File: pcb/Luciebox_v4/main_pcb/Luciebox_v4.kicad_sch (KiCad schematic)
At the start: 67 parts, among them J1 USB_B_Mini, P1 Power, P2 Analog, P3 Digital, P4 Digital, P5 CONN_01X01, P6 CONN_01X01, P7 CONN_01X01, P8 CONN_01X01, Q1 N-Channel_Mosfet, T1 terminal_3x1, T10 terminal_8x1, T11 terminal_8x1, T12 terminal_8x1, T13 terminal_8x1, T2 terminal_3x1, T3 terminal_3x1, T4 terminal_3x1, T5 terminal_8x1, T6 terminal_8x1, T7 terminal_3x1, T8 terminal_3x1, T9 terminal_3x1, U1 CA56-12SRWA, U2 8X8PADS, U3 ATmega328-PU, Y1 16MHz

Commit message: V4 main pcb ready for layouting
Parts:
- removed P1: Power, Socket_Arduino_Uno:Socket_Strip_Arduino_1x08, symbol Luciebox_components:Conn_01x08-Connector_Generic
- removed P2: Analog, Socket_Arduino_Uno:Socket_Strip_Arduino_1x06, symbol Luciebox_components:Conn_01x06-Connector_Generic
- removed P3: Digital, Socket_Arduino_Uno:Socket_Strip_Arduino_1x10, symbol Luciebox_components:Conn_01x10-Connector_Generic
- removed P4: Digital, Socket_Arduino_Uno:Socket_Strip_Arduino_1x08, symbol Luciebox_components:Conn_01x08-Connector_Generic
- removed P5, P6, P7, P8: CONN_01X01, Socket_Arduino_Uno:Arduino_1pin, symbol Luciebox_components:Conn_01x01-Connector_Generic
- removed Q1: N-Channel_Mosfet, Luciebox:TO-220-3, symbol Luciebox_components:N-Channel_Mosfet
- removed R1, R11, R12, R13, R14, R2, R3, R4, R5, R6, R7, R8, R9: 10K, Luciebox:1206_0805, symbol Luciebox_components:R_Small-Device
- removed R10: 100K, Luciebox:1206_0805, symbol Luciebox_components:R_Small-Device
- removed R_0_if_no_touch1: 0, Luciebox:1206_0805, symbol Luciebox_components:R_Small-Device
- removed S2: selector_knob, Luciebox:Rotary_Switch, symbol Luciebox_components:selector_knob
- removed T10, T11: terminal_8x1, Luciebox:Terminal_8x1_100mil, symbol Luciebox_components:terminal_8x1
- removed T2, T3, T4, T7, T8: terminal_3x1, Luciebox:Terminal_3x1_100mil, symbol Luciebox_components:terminal_3x1
- removed TP1: TestPoint_Probe, symbol Connector:TestPoint_Probe
- added A1: Arduino_UNO_R3, Module:Arduino_UNO_R3, symbol Luciebox_components:Arduino_UNO_R3
- added D1, D10, D2, D3, D4, D5, D6, D7, D8: D_Schottky, Luciebox:D_SMA, symbol Luciebox_components:D_Schottky
- added Q1: P-Channel MOSFET, Package_TO_SOT_SMD:SOT-23, symbol Luciebox_components:P-Channel MOSFET
- added Q2: NPN transistor, Luciebox:SOT-23, symbol Luciebox_components:NPN transistor
- added R10, R11, R12, R13, R15, R16, R17, R18, R20, R21, R22, R23, R6, R7, R8, R9: R_Small, Luciebox:0603_1608Metric, symbol Luciebox_components:R_Small
- added R25, R28: 100K, Luciebox:0603_1608Metric, symbol Luciebox_components:R_Small-Device
- added R26: 1K, Luciebox:0603_1608Metric, symbol Luciebox_components:R_Small-Device
- added R27: 10K, Luciebox:0603_1608Metric, symbol Luciebox_components:R_Small-Device
- added R_0_if_no_auto_power_off1: 0, Luciebox:0603_1608Metric, symbol Luciebox_components:R_Small-Device
- added T6: terminal_8x1, Luciebox:Terminal_8x1_100mil, symbol Luciebox_components:terminal_8x1
- C1, C2, C3: footprint Luciebox:0805 -> Luciebox:0603_1608Metric
- D9: renamed from D1; footprint Luciebox:smd_throughhole_2_pins -> Luciebox:D_SMA
- R1: renamed from R15; footprint Luciebox:1206_0805 -> Luciebox:0603_1608Metric
- R19: renamed from R20; footprint Luciebox:1206_0805 -> Luciebox:0603_1608Metric
- R2: renamed from R16; footprint Luciebox:1206_0805 -> Luciebox:0603_1608Metric
- R3: renamed from R17; footprint Luciebox:1206_0805 -> Luciebox:0603_1608Metric
- R4: renamed from R18; footprint Luciebox:1206_0805 -> Luciebox:0603_1608Metric
- R5: renamed from R19; footprint Luciebox:1206_0805 -> Luciebox:0603_1608Metric
- R_0_if_no_usb_switch1, R_reset_pullup1, R_vcc_protected1: footprint Luciebox:1206_0805 -> Luciebox:0603_1608Metric
- renumbered H5 to H2, H6 to H3, H2 to H4, H3 to H5, H7 to H6, H4 to H7, T5 to T1, T1 to T2, T6 to T4, T9 to T5, T13 to T7, T12 to T8
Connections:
- net +3V3: now also A1.4 (3V3)
- net 0(Rx): now also A1.15 (D0/RX), D5.1 (K); no longer T1.5
- net 1(Tx): now also A1.16 (D1/TX), D6.1 (K); no longer T4.6
- net 10(PWM-SS): now also A1.25 (D10)
- net 11(PWM-MOSI): now also A1.26 (D11)
- net 12(MISO): now also A1.27 (D12), D8.1 (K); no longer T1.7
- net 13(SCK): now also A1.28 (D13), D7.1 (K); no longer T4.8
- net 2: now also A1.17 (D2)
- net 3(PWM): now also A1.18 (D3)
- net 4: now also A1.19 (D4), D3.1 (K); no longer T4.7
- net 5(PWM): now also A1.20 (D5)
- net 6(PWM): now also A1.21 (D6)
- net 7: now also A1.22 (D7), D1.1 (K); no longer T1.8
- net 8: now also A1.23 (D8), D4.1 (K); no longer T1.6
- net 9(PWM): now also A1.24 (D9)
- net A0: now also A1.9 (A0), T6.6
- net A1: now also A1.10 (A1), R15.1, R20.1; no longer T1.3
- net A2: now also A1.11 (A2), R10.1, R6.1; no longer T4.3
- net A3: now also A1.12 (A3), D2.1 (K); no longer T4.5
- net A4(SDA): now also A1.13 (SDA/A4), A1.31 (SDA/A4)
- net A5(SCL): now also T2.3, A1.14 (SCL/A5), A1.32 (SCL/A5)
- net AREF: now also A1.30 (AREF)
- net GND: now also T8.7, A1.29 (GND), A1.6 (GND), A1.7 (GND), Q2.3 (E), R13.2, R23.2, R28.1, T6.1, T6.4; no longer T1.1, T2.3, T4.1, T8.8
- net IOREF: now also A1.2 (IOREF)
- net Reset: now also A1.3 (~{RESET})
- net VCC: now also T8.8, Q1.3 (D), R_0_if_no_auto_power_off1.1, T6.2; no longer R_0_if_no_usb_switch1.2, T8.1, T8.6
- net VCC_minimalCurrent: no longer T1.2, T4.2
- net Vin: now also R_0_if_no_usb_switch1.2, T8.1, T8.6, A1.8 (VIN), Q1.2 (S), R25.1, R_0_if_no_auto_power_off1.2
- net at T8.3: now also D10.2 (A), T6.5; no longer T8.5
- new net: D8.2 (A), T1.8
- new net: Q2.2 (B), R26.1, R27.2
- new net: R26.2, T6.7
- new net: Q1.1 (G), Q2.1 (C), R25.2
- new net: R18.2, T4.1
- new net: R17.2, T4.2
- new net: R16.2, T4.3
- new net: R15.2, T4.4
- new net: R9.2, T4.5
- new net: R8.2, T4.6
- new net: R7.2, T4.7
- new net: R6.2, T4.8
- new net: D6.2 (A), T1.6
- new net: R17.1, R21.2, R22.1
- new net: D1.2 (A), T1.1
- new net: D2.2 (A), T1.2
- new net: D3.2 (A), T1.3
- new net: D4.2 (A), T1.4
- new net: D5.2 (A), T1.5
- new net: D7.2 (A), T1.7
- new net: R12.2, R13.1, R9.1
- new net: R18.1, R22.2, R23.1
- new net: R11.2, R12.1, R8.1
- new net: R16.1, R20.2, R21.1
- new net: R10.2, R11.1, R7.1
- new net: D10.1 (K), T8.5
- new net: R1.1, T6.3
- new net 5V arduino: A1.5 (+5V)
- new net A4: R27.1, R28.2
- no-connect marks 5 -> 0
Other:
- removed sheet Luciebox_buttons
- note added: "Arduino UNO R3 Footprint"
- note added: "Button lights Common Anode"
- note removed: "1"
- note removed: "GND-SWITCHED"
- note removed: "Holes"
- note removed: "Shield for Arduino that uses the same pin disposition like "Uno" board Rev 3."
- note removed: "Touch ON and Auto power OFF"
- moved on the sheet: BZ1, C1, D9, H1, H2, H3, H4, H5, H6, H7, H8, J1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

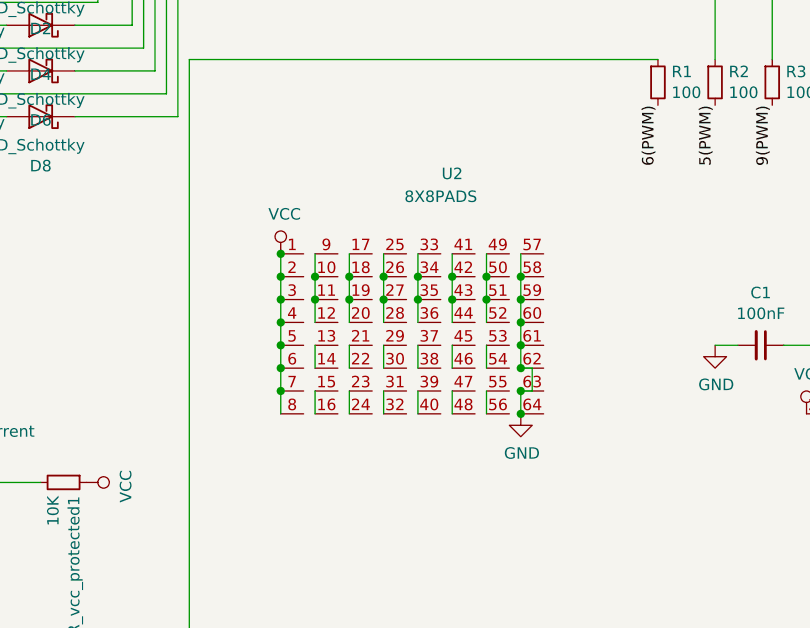
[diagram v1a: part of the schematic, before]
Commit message: layout main board start
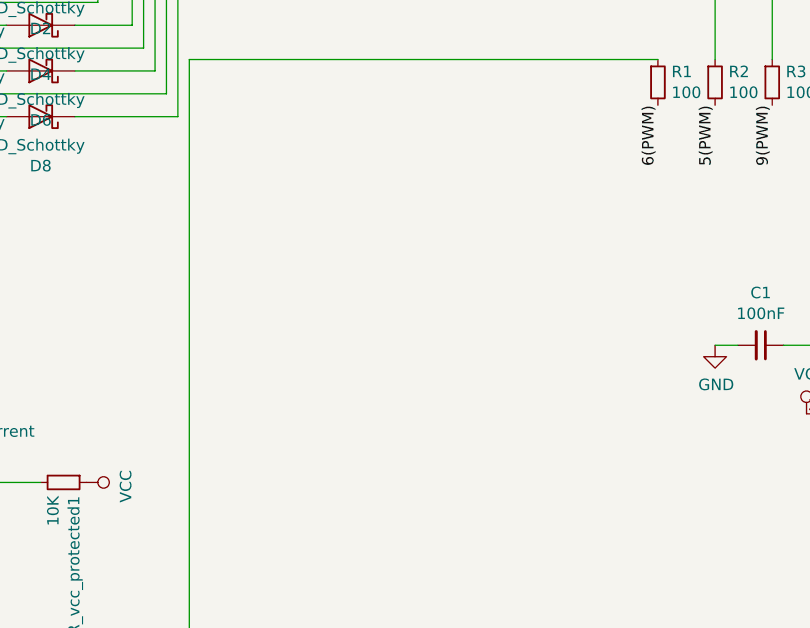
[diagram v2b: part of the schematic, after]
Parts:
- removed U2: 8X8PADS, Luciebox:64_PADS_100mil, symbol Luciebox_components:8X8PADS

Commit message: Pcb v4 evolution
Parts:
- added J2: USB_B_Mini, Luciebox:usb_mini_Molex-0548190519, symbol Luciebox_components:USB_B_Mini
- A1: footprint Module:Arduino_UNO_R3 -> Module:Arduino_UNO_R3_WithMountingHoles
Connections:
- net A4: now also R27.2; no longer R27.1, R28.2
- net GND: now also J2.1 (GND), J2.6 (Shield)
- net at Q2.2 (B), R26.1: now also R27.1, R28.2; no longer R27.2
- net at J1.2 (ID), T5.1: now also J2.2 (ID)
- net at J1.3 (D+), T5.3: now also J2.3 (D+)
- net at J1.4 (D-), T5.2: now also J2.4 (D-)
- net at D9.2 (A), J1.5 (VBUS): now also J2.5 (VBUS)
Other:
- moved on the sheet: R27, T5

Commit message: Delete Arduino Uno footprint. Line up bottonboard and main pcb
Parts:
- removed A1: Arduino_UNO_R3, Module:Arduino_UNO_R3_WithMountingHoles, symbol Luciebox_components:Arduino_UNO_R3
- removed H4, H5, H7, H8: MountingHole, Luciebox:MountingHole_4.3mm_M4, symbol Luciebox_components:MountingHole
- added U2: 8X8PADS, Luciebox:8X8PADS_100mil, symbol Luciebox_components:8X8PADS
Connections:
- net GND: now also U2.57, U2.58, U2.59, U2.60, U2.61, U2.62, U2.63, U2.64
- net VCC: now also U2.1, U2.2, U2.3, U2.4, U2.5, U2.6, U2.7, U2.8
- new net: U2.10, U2.9
- new net: U2.11, U2.12
- new net: U2.13, U2.14, U2.15, U2.16
- new net: U2.17, U2.18
- new net: U2.19, U2.20
- new net: U2.21, U2.22, U2.23, U2.24
- new net: U2.30, U2.31, U2.32
- new net: U2.38, U2.39, U2.40
- new net: U2.46, U2.47, U2.48
- new net: U2.54, U2.55, U2.56
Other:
- note removed: "Arduino UNO R3 Footprint"

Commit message: Moved boards connector. Main board ready for traces.
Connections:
- net VCC: no longer U2.8
- net at U2.13, U2.14, U2.15: no longer U2.16
- net at U2.21, U2.22, U2.23: no longer U2.24
- net at U2.25: now also U2.26
- net at U2.27: now also U2.28
- net at U2.29: now also U2.30, U2.31
- net at U2.33: now also U2.34
- net at U2.35: now also U2.36
- net at U2.37: now also U2.38, U2.39, U2.40
- net at U2.41: now also U2.42
- net at U2.43: now also U2.44
- net at U2.45: now also U2.46, U2.47, U2.48
- net at U2.49: now also U2.50
- net at U2.51: now also U2.52
- net at U2.53: now also U2.54, U2.55, U2.56
- now unconnected: U2.32

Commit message: Main board traced
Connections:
- net at J1.2 (ID), T5.1: no longer J2.2 (ID)
- net at J1.3 (D+), T5.3: no longer J2.3 (D+)
- net at J1.4 (D-), T5.2: no longer J2.4 (D-)
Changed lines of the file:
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@@
 (kicad_sch (version 20211123) (generator eeschema)
   (paper "A4")
-  (junction (at 175.26 143.51) (diameter 0) (color 0 0 0 0)
-  )
   (junction (at 255.27 134.62) (diameter 0) (color 0 0 0 0)
   )
@@
   (junction (at 49.53 90.17) (diameter 0) (color 0 0 0 0)
   )
-  (junction (at 173.99 146.05) (diameter 0) (color 0 0 0 0)
-  )
   (junction (at 137.16 180.34) (diameter 0) (color 0 0 0 0)
   )
@@
   (junction (at 48.26 160.02) (diameter 0) (color 0 0 0 0)
   )
-  (junction (at 171.45 148.59) (diameter 0) (color 0 0 0 0)
-  )
   (junction (at 172.72 153.67) (diameter 0) (color 0 0 0 0)
   )
@@
     (stroke (width 0) (type default) (color 0 0 0 0))
   )
-  (wire (pts (xy 173.99 121.92) (xy 173.99 146.05))
-    (stroke (width 0) (type default) (color 0 0 0 0))
-  )
   (wire (pts (xy 48.26 160.02) (xy 53.34 160.02))
     (stroke (width 0) (type default) (color 0 0 0 0))
@@
     (stroke (width 0) (type default) (color 0 0 0 0))
   )
-  (wire (pts (xy 168.91 124.46) (xy 171.45 124.46))
-    (stroke (width 0) (type default) (color 0 0 0 0))
-  )
   (wire (pts (xy 82.55 148.59) (xy 82.55 160.02))
     (stroke (width 0) (type default) (color 0 0 0 0))
@@
     (stroke (width 0) (type default) (color 0 0 0 0))
   )
-  (wire (pts (xy 171.45 124.46) (xy 171.45 148.59))
-    (stroke (width 0) (type default) (color 0 0 0 0))
-  )
   (wire (pts (xy 102.87 181.61) (xy 107.95 181.61))
     (stroke (width 0) (type default) (color 0 0 0 0))
@@
     (stroke (width 0) (type default) (color 0 0 0 0))
   )
-  (wire (pts (xy 168.91 148.59) (xy 171.45 148.59))
-    (stroke (width 0) (type default) (color 0 0 0 0))
-  )
   (wire (pts (xy 254 41.91) (xy 254 44.45))
     (stroke (width 0) (type default) (color 0 0 0 0))
@@
     (stroke (width 0) (type default) (color 0 0 0 0))
   )
-  (wire (pts (xy 180.34 143.51) (xy 175.26 143.51))
+  (wire (pts (xy 168.91 143.51) (xy 180.34 143.51))
     (stroke (width 0) (type default) (color 0 0 0 0))
   )
@@
     (stroke (width 0) (type default) (color 0 0 0 0))
   )
-  (wire (pts (xy 175.26 143.51) (xy 168.91 143.51))
-    (stroke (width 0) (type default) (color 0 0 0 0))
-  )
   (wire (pts (xy 242.57 36.83) (xy 242.57 39.37))
     (stroke (width 0) (type default) (color 0 0 0 0))
@@
     (stroke (width 0) (type default) (color 0 0 0 0))
   )
-  (wire (pts (xy 171.45 148.59) (xy 180.34 148.59))
+  (wire (pts (xy 168.91 148.59) (xy 180.34 148.59))
     (stroke (width 0) (type default) (color 0 0 0 0))
   )
@@
     (stroke (width 0) (type default) (color 0 0 0 0))
   )
-  (wire (pts (xy 168.91 146.05) (xy 173.99 146.05))
-    (stroke (width 0) (type default) (color 0 0 0 0))
-  )
   (wire (pts (xy 250.19 36.83) (xy 250.19 39.37))
     (stroke (width 0) (type default) (color 0 0 0 0))
@@
     (stroke (width 0) (type default) (color 0 0 0 0))
   )
-  (wire (pts (xy 168.91 121.92) (xy 173.99 121.92))
-    (stroke (width 0) (type default) (color 0 0 0 0))
-  )
-  (wire (pts (xy 168.91 119.38) (xy 175.26 119.38))
-    (stroke (width 0) (type default) (color 0 0 0 0))
-  )
   (wire (pts (xy 87.63 97.79) (xy 73.66 97.79))
     (stroke (width 0) (type default) (color 0 0 0 0))
@@
     (stroke (width 0) (type default) (color 0 0 0 0))
   )
-  (wire (pts (xy 175.26 119.38) (xy 175.26 143.51))
-    (stroke (width 0) (type default) (color 0 0 0 0))
-  )
   (wire (pts (xy 139.7 137.16) (xy 139.7 177.8))
     (stroke (width 0) (type default) (color 0 0 0 0))
@@
     (stroke (width 0) (type default) (color 0 0 0 0))
   )
-  (wire (pts (xy 180.34 146.05) (xy 173.99 146.05))
-    (stroke (width 0) (type default) (color 0 0 0 0))
-  )
+  (wire (pts (xy 168.91 146.05) (xy 180.34 146.05))
+    (stroke (width 0) (type default) (color 0 0 0 0))
+  )
